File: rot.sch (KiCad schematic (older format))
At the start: 34 parts, among them J3 543630489, J4 M20-7830642, U2 W25Q32JVSSIQ_TR, U3 W25Q32JVSSIQ_TR, U4 W25Q32JVSSIQ_TR, U5 W25Q32JVSSIQ_TR

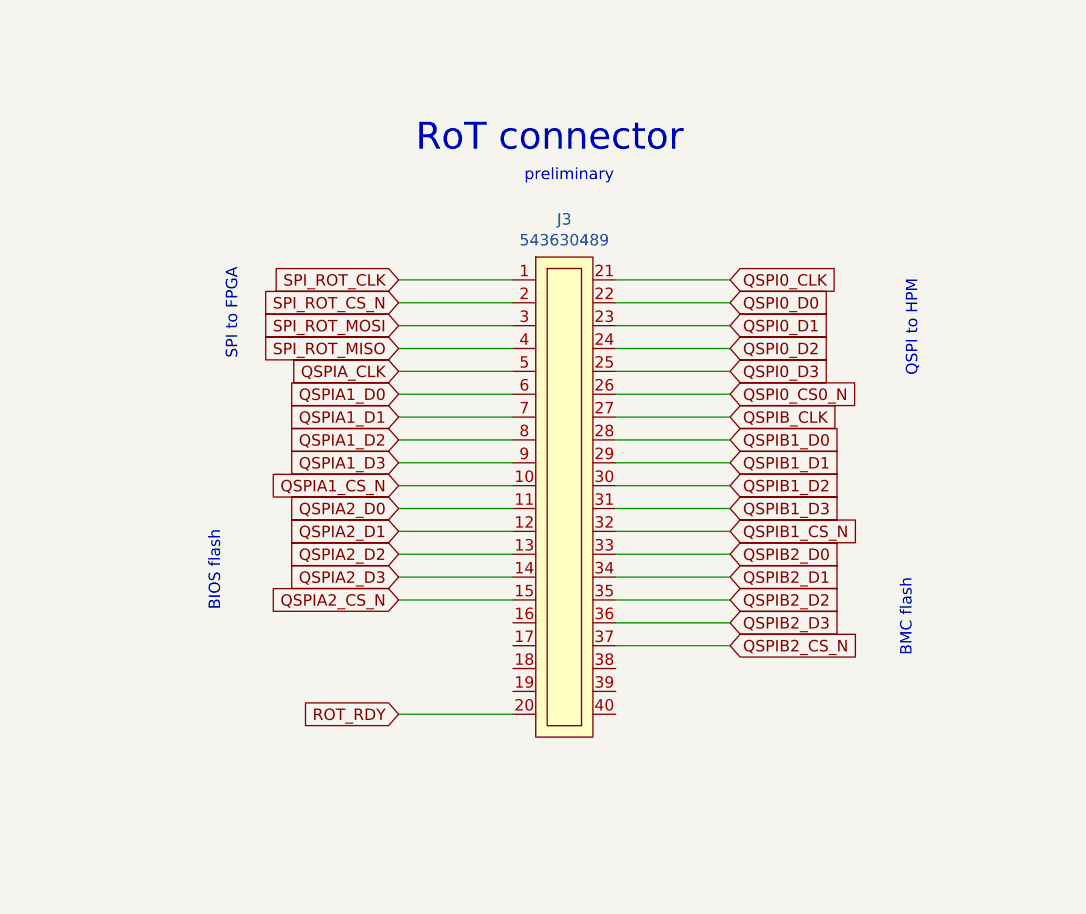
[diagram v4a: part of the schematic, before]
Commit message: Updated RoT and FLASH connections
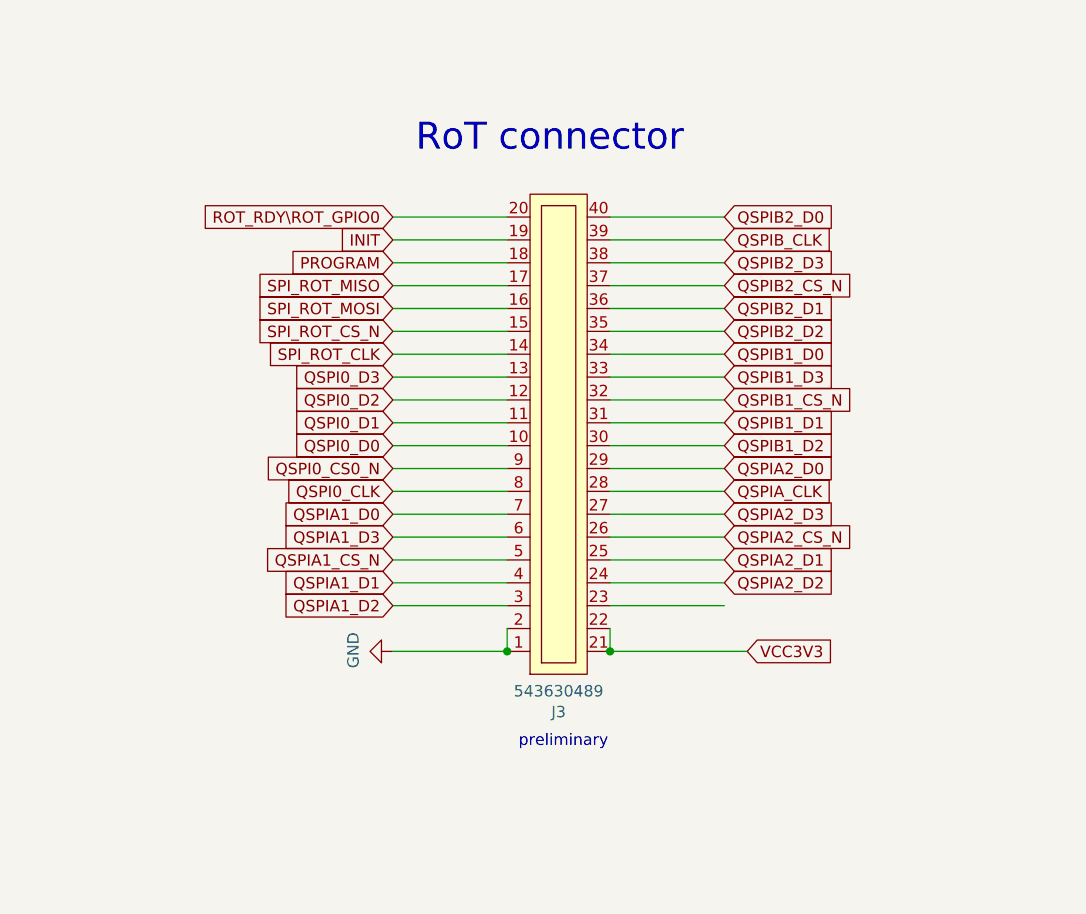
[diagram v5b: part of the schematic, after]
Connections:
- net GND: now also J3.1, J3.2
- net QSPI0_CLK: now also J3.8; no longer J3.21
- net QSPI0_CS0_N: now also J3.9; no longer J3.26
- net QSPI0_D0: now also J3.10; no longer J3.22
- net QSPI0_D1: now also J3.11; no longer J3.23
- net QSPI0_D2: now also J3.12; no longer J3.24
- net QSPI0_D3: now also J3.13; no longer J3.25
- net QSPIA1_CS_N: now also J3.5; no longer J3.10
- net QSPIA1_D0: now also J3.7; no longer J3.6
- net QSPIA1_D1: now also J3.4; no longer J3.7
- net QSPIA1_D2: now also J3.3; no longer J3.8
- net QSPIA1_D3: now also J3.6; no longer J3.9
- net QSPIA2_CS_N: now also J3.26; no longer J3.15
- net QSPIA2_D0: now also J3.29; no longer J3.11
- net QSPIA2_D1: now also J3.25; no longer J3.12
- net QSPIA2_D2: now also J3.24; no longer J3.13
- net QSPIA2_D3: now also J3.27; no longer J3.14
- net QSPIA_CLK: now also J3.28; no longer J3.5
- net QSPIB1_D0: now also J3.34; no longer J3.28
- net QSPIB1_D1: now also J3.31; no longer J3.29
- net QSPIB1_D3: now also J3.33; no longer J3.31
- net QSPIB2_D0: now also J3.40; no longer J3.33
- net QSPIB2_D1: now also J3.36; no longer J3.34
- net QSPIB2_D3: now also J3.38; no longer J3.36
- net QSPIB_CLK: now also J3.39; no longer J3.27
- net SPI_ROT_CLK: now also J3.14; no longer J3.1
- net SPI_ROT_CS_N: now also J3.15; no longer J3.2
- net SPI_ROT_MISO: now also J3.17; no longer J3.4
- net SPI_ROT_MOSI: now also J3.16; no longer J3.3
- net VCC3V3: now also J3.21, J3.22
- net PROGRAM: now reaches J3.18
- net INIT: now reaches J3.19
- net ROT_RDY renamed ROT_RDY\ROT_GPIO0
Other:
- note removed: "QSPI to HPM"
- note removed: "SPI to FPGA\n"
- moved on the sheet: J3
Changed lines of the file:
@@
 $Descr A3 16535 11693
 encoding utf-8
-Sheet 4 10
+Sheet 8 10
 Title ""
 Date ""
@@
 L artix-dc-scm:543630489 J3
 U 1 1 6268C044
-P 8950 4650
-F 0 "J3" H 8975 4665 50  0000 C CNN
-F 1 "543630489" H 8975 4574 50  0000 C CNN
-F 2 "artix-dc-scm-footprints:543630489" H 8700 2300 50  0001 C CNN
-F 3 "https://www.molex.com/pdm_docs/sd/543630489_sd.pdf" H 9200 2350 50  0001 C CNN
-	1    8950 4650
-	1    0    0    -1
-$EndComp
-Wire Wire Line
-	8750 4900 8250 4900
-Wire Wire Line
-	8750 5000 8250 5000
+P 8925 6775
+F 0 "J3" H 8950 6790 50  0000 C CNN
+F 1 "543630489" H 8950 6699 50  0000 C CNN
+F 2 "artix-dc-scm-footprints:543630489" H 8675 4425 50  0001 C CNN
+F 3 "https://www.molex.com/pdm_docs/sd/543630489_sd.pdf" H 9175 4475 50  0001 C CNN
+	1    8925 6775
+	1    0    0    1
+$EndComp
+Wire Wire Line
+	8725 6325 8225 6325
+Wire Wire Line
+	8725 6225 8225 6225
 Text GLabel 1950 2550 0    50   Input ~ 0
 QSPIA1_CS_N
@@
 Text Notes 1475 1475 0    50   ~ 0
 One or typically two flash devices used to contain the BIOS firmware image
-Text GLabel 8250 4900 0    50   Input ~ 0
+Text GLabel 8225 5225 0    50   Input ~ 0
 SPI_ROT_CLK
-Text GLabel 8250 5000 0    50   Input ~ 0
+Text GLabel 8225 5125 0    50   Input ~ 0
 SPI_ROT_CS_N
-Text GLabel 8250 5100 0    50   Input ~ 0
+Text GLabel 8225 5025 0    50   Input ~ 0
 SPI_ROT_MOSI
-Text GLabel 8250 5200 0    50   Input ~ 0
+Text GLabel 8225 4925 0    50   Input ~ 0
 SPI_ROT_MISO
 Wire Wire Line
-	8750 5100 8250 5100
-Wire Wire Line
-	8750 5200 8250 5200
-Text GLabel 8250 5800 0    50   Input ~ 0
+	8725 6125 8225 6125
+Wire Wire Line
+	8725 6025 8225 6025
+Text GLabel 8225 6125 0    50   Input ~ 0
 QSPIA1_CS_N
-Text GLabel 8250 5300 0    50   Input ~ 0
+Text GLabel 9675 5825 2    50   Input ~ 0
 QSPIA_CLK
-Text GLabel 8250 5400 0    50   Input ~ 0
+Text GLabel 8225 5925 0    50   Input ~ 0
 QSPIA1_D0
-Text GLabel 8250 5600 0    50   Input ~ 0
+Text GLabel 8225 6325 0    50   Input ~ 0
 QSPIA1_D2
-Text GLabel 8250 5700 0    50   Input ~ 0
+Text GLabel 8225 6025 0    50   Input ~ 0
 QSPIA1_D3
-Text GLabel 8250 6300 0    50   Input ~ 0
+Text GLabel 9675 6025 2    50   Input ~ 0
 QSPIA2_CS_N
-Text GLabel 8250 5900 0    50   Input ~ 0
+Text GLabel 9675 5725 2    50   Input ~ 0
 QSPIA2_D0
-Text GLabel 8250 6100 0    50   Input ~ 0
+Text GLabel 9675 6225 2    50   Input ~ 0
 QSPIA2_D2
-Text GLabel 8250 6200 0    50   Input ~ 0
+Text GLabel 9675 5925 2    50   Input ~ 0
 QSPIA2_D3
-Text GLabel 9700 6000 2    50   Input ~ 0
+Text GLabel 9675 5425 2    50   Input ~ 0
 QSPIB1_CS_N
-Text GLabel 9700 5500 2    50   Input ~ 0
+Text GLabel 9675 4725 2    50   Input ~ 0
 QSPIB_CLK
-Text GLabel 9700 5600 2    50   Input ~ 0
+Text GLabel 9675 5225 2    50   Input ~ 0
 QSPIB1_D0
-Text GLabel 9700 5800 2    50   Input ~ 0
+Text GLabel 9675 5625 2    50   Input ~ 0
 QSPIB1_D2
-Text GLabel 9700 5900 2    50   Input ~ 0
+Text GLabel 9675 5325 2    50   Input ~ 0
 QSPIB1_D3
-Text GLabel 9700 6500 2    50   Input ~ 0
+Text GLabel 9675 4925 2    50   Input ~ 0
 QSPIB2_CS_N
-Text GLabel 9700 6100 2    50   Input ~ 0
+Text GLabel 9675 4625 2    50   Input ~ 0
 QSPIB2_D0
-Text GLabel 9700 6300 2    50   Input ~ 0
+Text GLabel 9675 5125 2    50   Input ~ 0
 QSPIB2_D2
-Text GLabel 9700 6400 2    50   Input ~ 0
+Text GLabel 9675 4825 2    50   Input ~ 0
 QSPIB2_D3
-Text GLabel 8250 5500 0    50   Input ~ 0
+Text GLabel 8225 6225 0    50   Input ~ 0
 QSPIA1_D1
-Text GLabel 8250 6000 0    50   Input ~ 0
+Text GLabel 9675 6125 2    50   Input ~ 0
 QSPIA2_D1
-Text GLabel 9700 5700 2    50   Input ~ 0
+Text GLabel 9675 5525 2    50   Input ~ 0
 QSPIB1_D1
-Text GLabel 9700 6200 2    50   Input ~ 0
+Text GLabel 9675 5025 2    50   Input ~ 0
 QSPIB2_D1
-Text GLabel 9700 4900 2    50   Input ~ 0
+Text GLabel 8225 5825 0    50   Input ~ 0
 QSPI0_CLK
-Text GLabel 9700 5400 2    50   Input ~ 0
+Text GLabel 8225 5725 0    50   Input ~ 0
 QSPI0_CS0_N
-Text GLabel 9700 5000 2    50   Input ~ 0
+Text GLabel 8225 5625 0    50   Input ~ 0
 QSPI0_D0
-Text GLabel 9700 5100 2    50   Input ~ 0
+Text GLabel 8225 5525 0    50   Input ~ 0
 QSPI0_D1
-Text GLabel 9700 5200 2    50   Input ~ 0
+Text GLabel 8225 5425 0    50   Input ~ 0
 QSPI0_D2
-Text GLabel 9700 5300 2    50   Input ~ 0
+Text GLabel 8225 5325 0    50   Input ~ 0
 QSPI0_D3
 Wire Wire Line
-	8250 5300 8750 5300
-Wire Wire Line
-	8750 5400 8250 5400
-Wire Wire Line
-	8750 5500 8250 5500
-Wire Wire Line
-	8750 5600 8250 5600
-Wire Wire Line
-	8750 5700 8250 5700
-Wire Wire Line
-	8750 5900 8250 5900
-Wire Wire Line
-	8750 6000 8250 6000
-Wire Wire Line
-	8750 6100 8250 6100
-Wire Wire Line
-	8750 6200 8250 6200
-Wire Wire Line
-	9200 5600 9700 5600
-Wire Wire Line
-	9200 5700 9700 5700
-Wire Wire Line
-	9200 5800 9700 5800
-Wire Wire Line
-	9200 5900 9700 5900
-Wire Wire Line
-	9200 6100 9700 6100
-Wire Wire Line
-	9200 6200 9700 6200
-Wire Wire Line
-	9200 6300 9700 6300
-Wire Wire Line
-	9200 6400 9700 6400
-Wire Wire Line
-	8750 6300 8250 6300
-Wire Wire Line
-	9200 5500 9700 5500
-Wire Wire Line
-	9200 6000 9700 6000
-Wire Wire Line
-	9200 6500 9700 6500
-Wire Wire Line
-	8750 5800 8250 5800
-Wire Wire Line
-	9700 4900 9200 4900
-Wire Wire Line
-	9700 5000 9200 5000
-Wire Wire Line
-	9700 5100 9200 5100
-Wire Wire Line
-	9700 5200 9200 5200
-Wire Wire Line
-	9700 5300 9200 5300
-Wire Wire Line
-	9700 5400 9200 5400
+	8225 5925 8725 5925
+Wire Wire Line
+	8725 5825 8225 5825
+Wire Wire Line
+	8725 5725 8225 5725
+Wire Wire Line
+	8725 5625 8225 5625
+Wire Wire Line
+	8725 5525 8225 5525
+Wire Wire Line
+	8725 5325 8225 5325
+Wire Wire Line
+	8725 5225 8225 5225
+Wire Wire Line
+	8725 5125 8225 5125
+Wire Wire Line
+	8725 5025 8225 5025
+Wire Wire Line
+	9175 5825 9675 5825
+Wire Wire Line
+	9175 5725 9675 5725
+Wire Wire Line
+	9175 5625 9675 5625
+Wire Wire Line
+	9175 5525 9675 5525
+Wire Wire Line
+	9175 5325 9675 5325
+Wire Wire Line
+	9175 5225 9675 5225
+Wire Wire Line
+	9175 5125 9675 5125
+Wire Wire Line
+	9175 5025 9675 5025
+Wire Wire Line
+	8725 4925 8225 4925
+Wire Wire Line
+	9175 5925 9675 5925
+Wire Wire Line
+	9175 5425 9675 5425
+Wire Wire Line
+	9175 4925 9675 4925
+Wire Wire Line
+	8725 5425 8225 5425
+Wire Wire Line
+	9675 6325 9175 6325
+Wire Wire Line
+	9675 6225 9175 6225
+Wire Wire Line
+	9675 6125 9175 6125
+Wire Wire Line
+	9675 6025 9175 6025
 Text Notes 8325 4350 0    118  ~ 0
 RoT connector
-Text Notes 8800 4475 0    50   ~ 0
+Text Notes 8775 6950 0    50   ~ 0
 preliminary\n
-Text Notes 7550 5250 1    50   ~ 0
-SPI to FPGA\n
-Text Notes 7475 6350 1    50   ~ 0
-BIOS flash
-Text Notes 10500 6550 1    50   ~ 0
-BMC flash
-Text Notes 10525 5325 1    50   ~ 0
-QSPI to HPM
-Text GLabel 8250 6800 0    50   Input ~ 0
-ROT_RDY
-Wire Wire Line
-	8750 6800 8250 6800
+Text GLabel 8225 4625 0    50   Input ~ 0
+ROT_RDY\ROT_GPIO0
 $Comp
 L artix-dc-scm:M20-7830642 J4
@@
 Text Notes 12325 2425 1    50   ~ 0
 TODO: tie this pins to DC-SCI connector
+Wire Wire Line
+	9675 4825 9175 4825
+Wire Wire Line
+	9675 4725 9175 4725
+Wire Wire Line
+	9675 4625 9175 4625
+Wire Wire Line
+	8725 4825 8225 4825
+Wire Wire Line
+	8725 4725 8225 4725
+Wire Wire Line
+	8725 4625 8225 4625
+Text GLabel 8225 4825 0    50   Input ~ 0
+PROGRAM
+Text GLabel 8225 4725 0    50   Input ~ 0
+INIT
+Text GLabel 9775 6525 2    50   Input ~ 0
+VCC3V3
+Wire Wire Line
+	8225 6525 8725 6525
+$Comp
+L artix-dc-scm:GND #PWR?
+U 1 1 626717FC
+P 8225 6525
+AR Path="/5FC6B687/626717FC" Ref="#PWR?"  Part="1"
+AR Path="/624C566F/626717FC" Ref="#PWR?"  Part="1"
+F 0 "#PWR?" H 8225 6275 50  0001 C CNN
+F 1 "GND" H 8230 6352 50  0000 C CNN
+F 2 "" H 8225 6525 50  0001 C CNN
+F 3 "" H 8225 6525 50  0001 C CNN
+	1    8225 6525
+	0    1    -1   0
+$EndComp
+Wire Wire Line
+	8725 6425 8725 6525
+Connection ~ 8725 6525
+Wire Wire Line
+	9175 6525 9775 6525
+Wire Wire Line
+	9175 6425 9175 6525
+Connection ~ 9175 6525
 $EndSCHEMATC

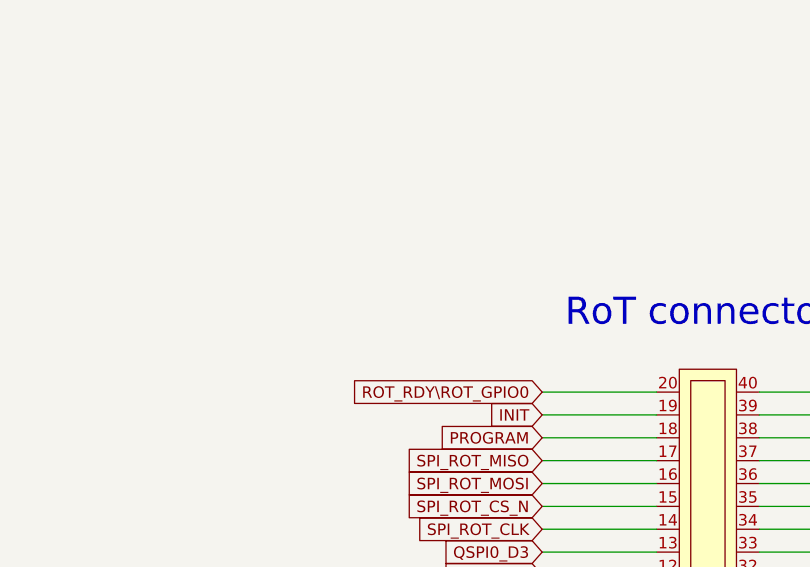
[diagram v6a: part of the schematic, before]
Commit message: Connected boot QSPI
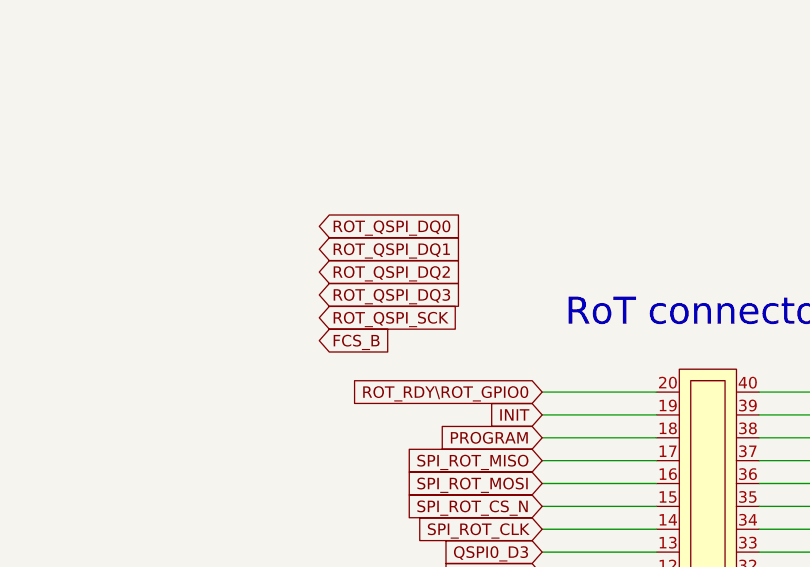
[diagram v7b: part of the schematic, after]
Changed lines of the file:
@@
 	9175 6425 9175 6525
 Connection ~ 9175 6525
+Text GLabel 7250 3900 2    50   Input ~ 0
+ROT_QSPI_DQ0
+Text GLabel 7250 4000 2    50   Input ~ 0
+ROT_QSPI_DQ1
+Text GLabel 7250 4100 2    50   Input ~ 0
+ROT_QSPI_DQ2
+Text GLabel 7250 4200 2    50   Input ~ 0
+ROT_QSPI_DQ3
+Text GLabel 7250 4300 2    50   Input ~ 0
+ROT_QSPI_SCK
+Text GLabel 7250 4400 2    50   Input ~ 0
+FCS_B
 $EndSCHEMATC
